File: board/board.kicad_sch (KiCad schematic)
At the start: 37 parts, among them J1 Conn_01x07_Pin, J2 Conn_01x06_Pin, J3 Conn_01x10_Pin, J4 Conn_01x08_Pin, J5 Conn_01x04_Socket, J6 Conn_01x04_Socket, J7 RJ45_Hanrun_HR911105A_Horizon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, J8 Conn_01x02_Pin, U1 7414, U2 AMS1117-3.3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

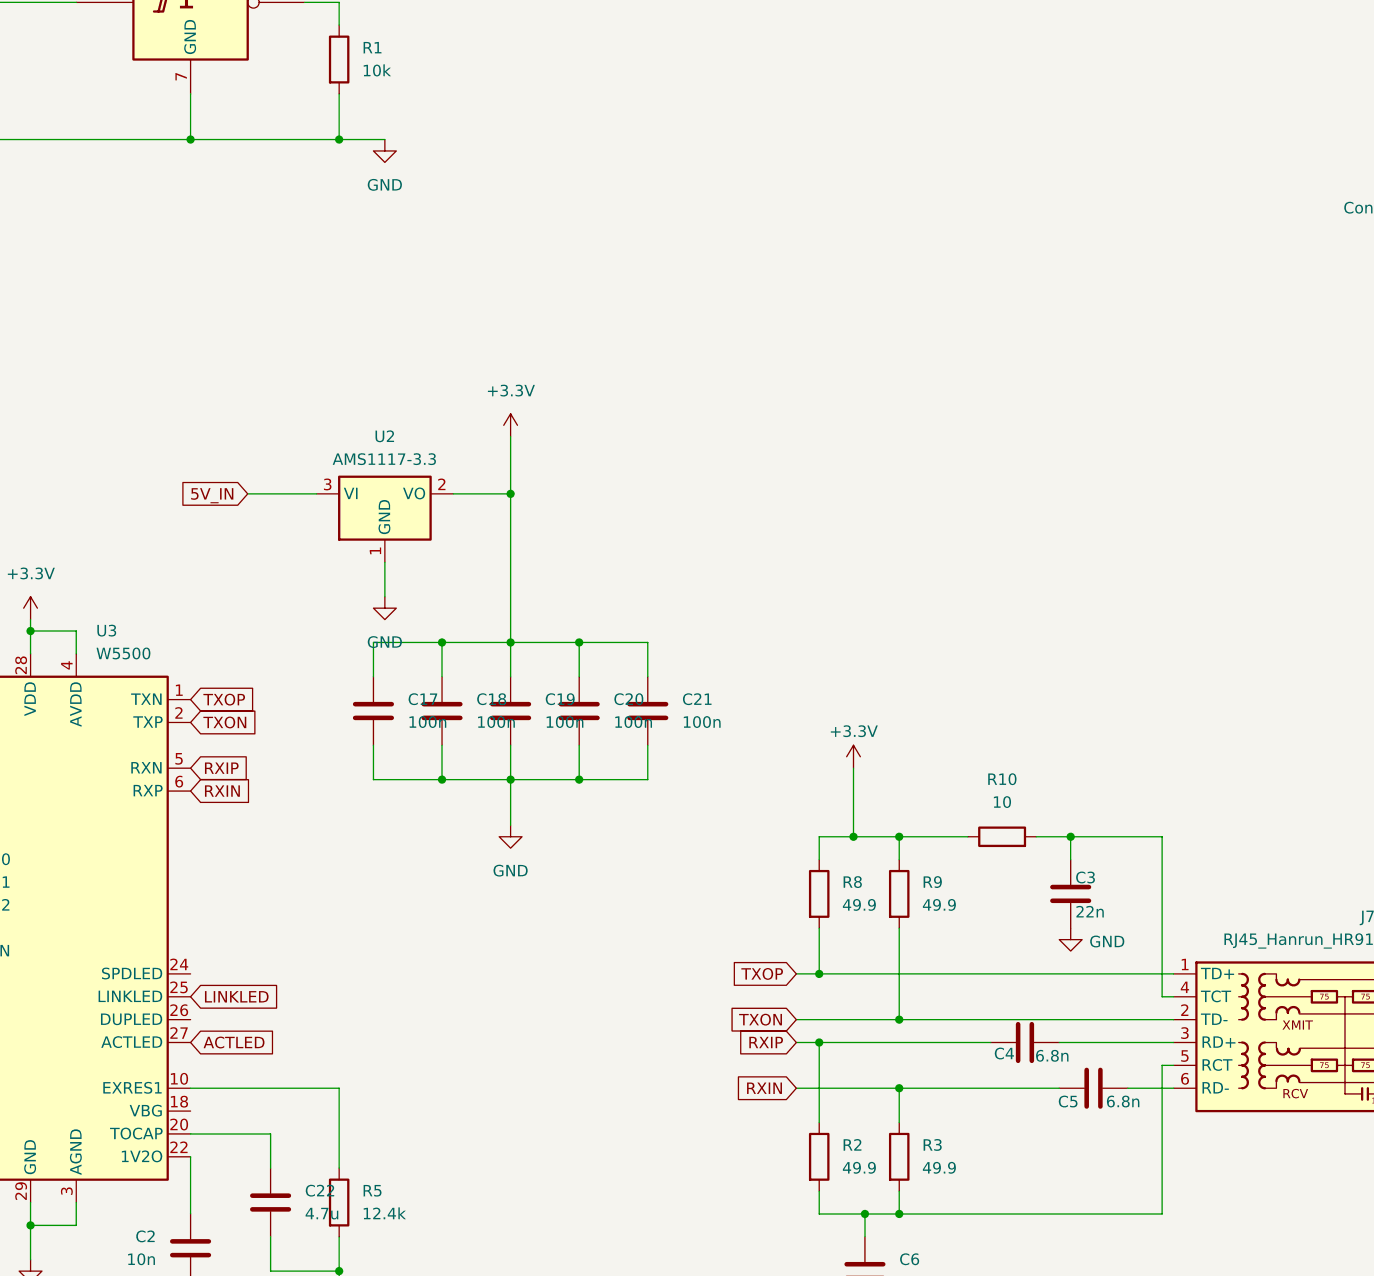
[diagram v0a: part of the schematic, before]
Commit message: Removal of C4 and C5 from Ethernet rx lines
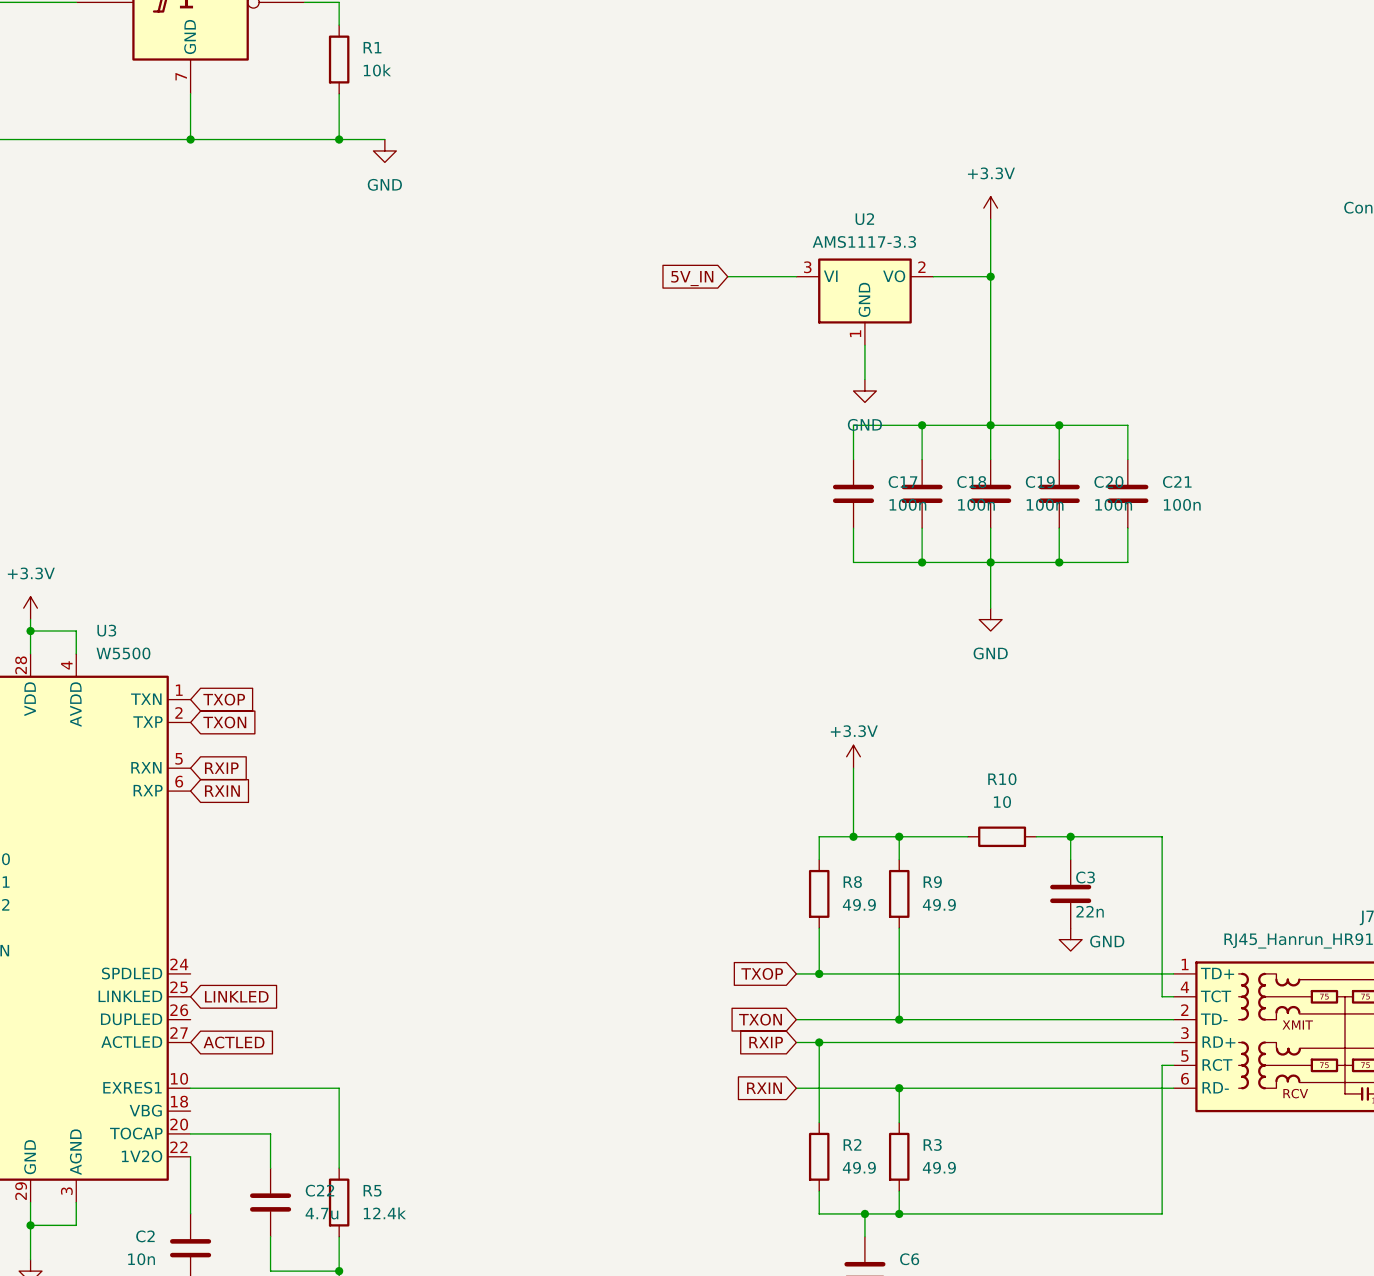
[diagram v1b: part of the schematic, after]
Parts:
- removed C4, C5: 6.8n, Capacitor_SMD:C_0603_1608Metric, symbol Device:C
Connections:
- net RXIN: now also J7.6 (RD-)
- net RXIP: now also J7.3 (RD+)
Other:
- moved on the sheet: C17, C18, C19, C20, C21, U2
